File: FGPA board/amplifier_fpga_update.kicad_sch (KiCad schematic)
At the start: 10 parts, among them U1 LFXP2-5E-5TN144, U3 MCP4921

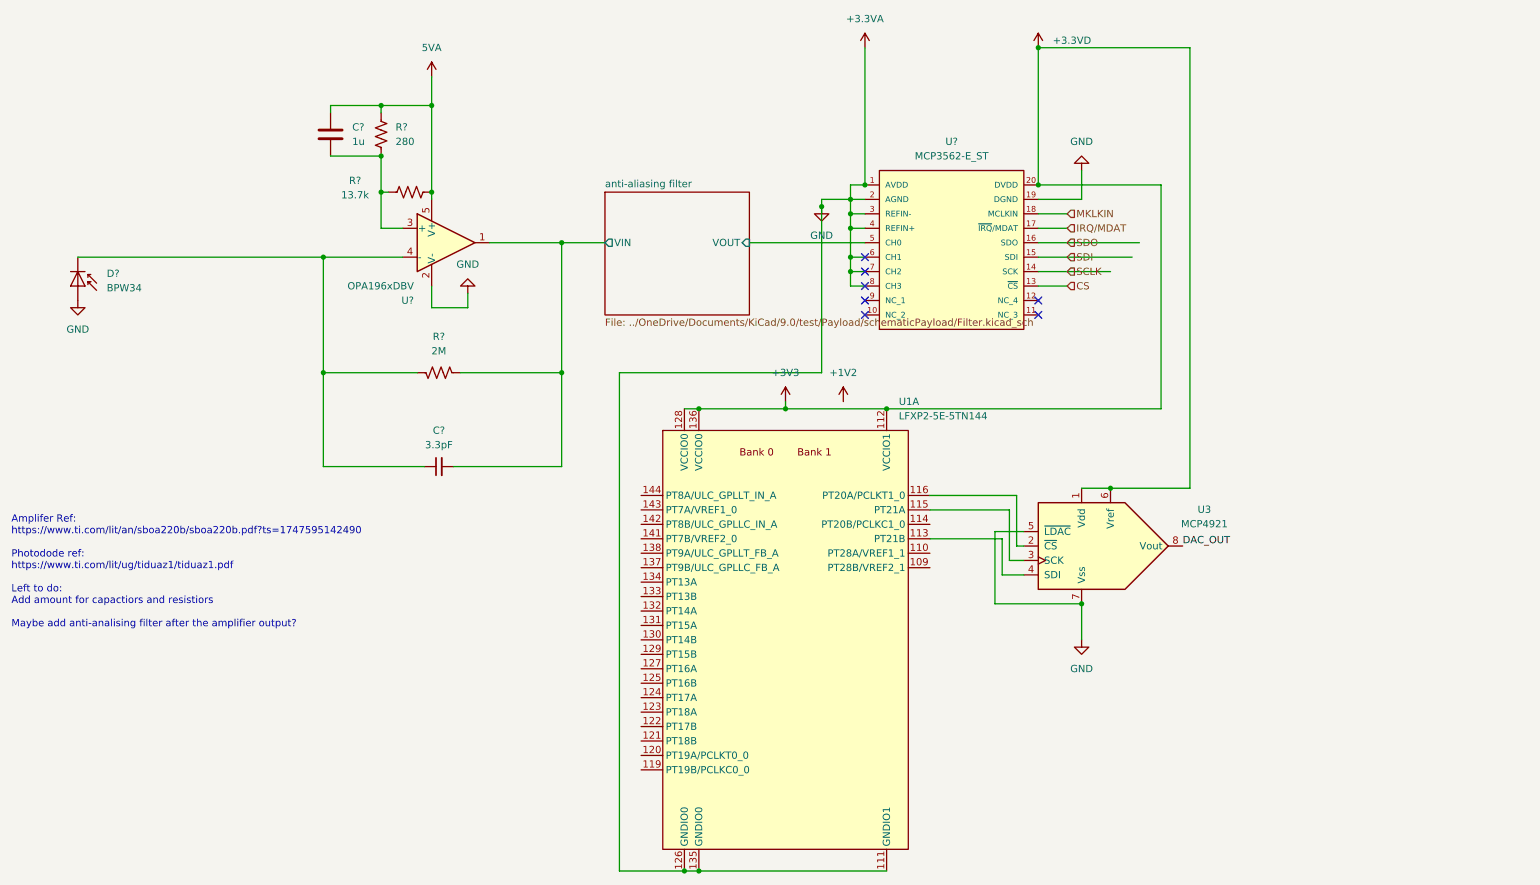
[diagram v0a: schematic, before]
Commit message: Add files via upload
Added SPI Flash, decoupling capacitors to ADC, decoupling to FPGA power pins and VCCPLL,
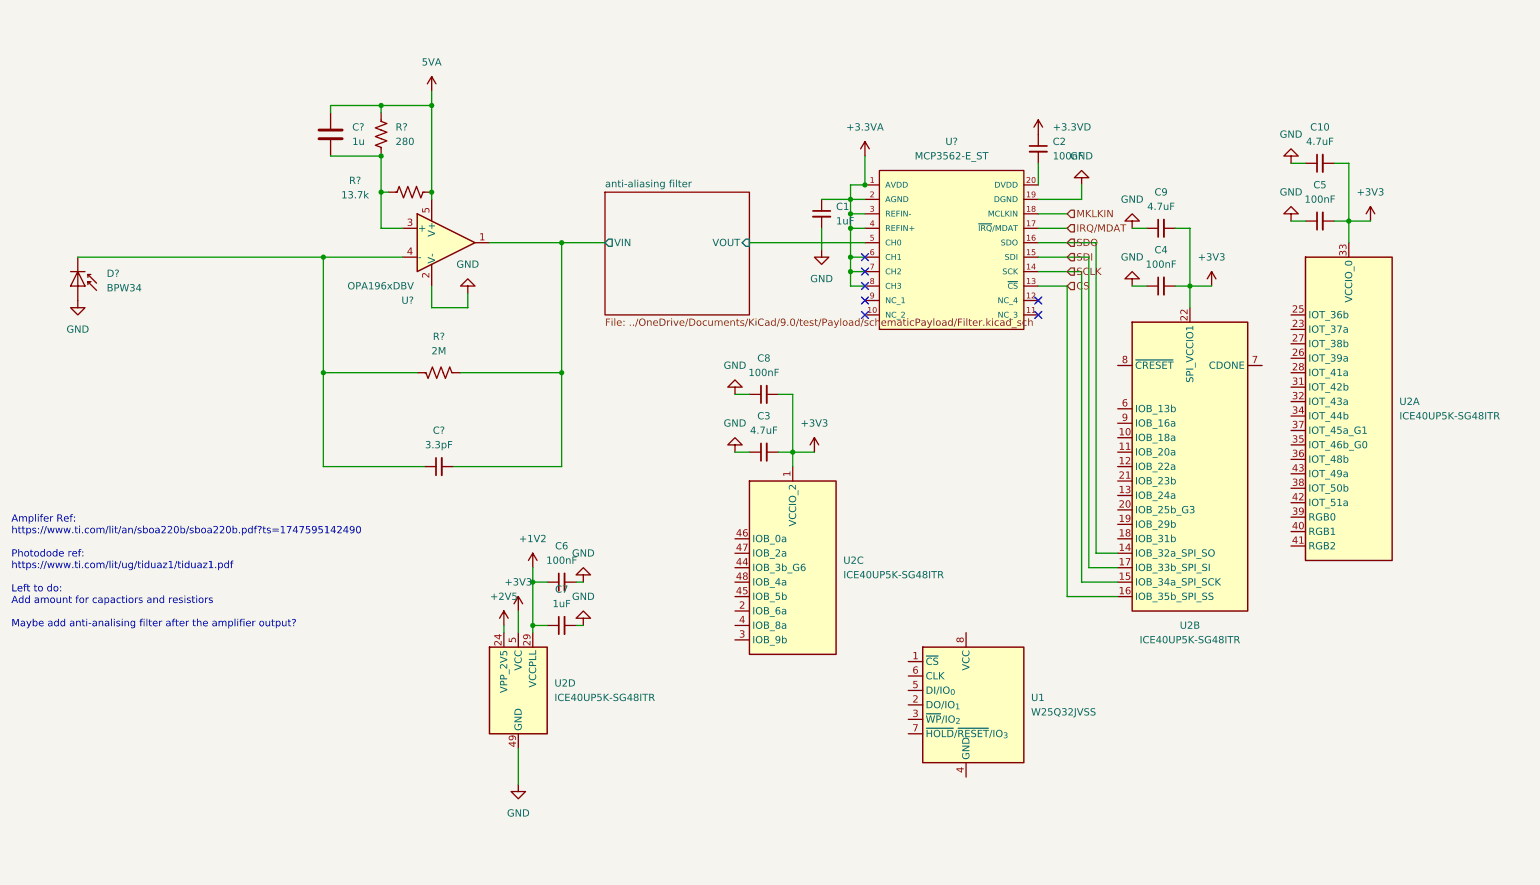
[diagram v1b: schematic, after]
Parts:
- removed U1: LFXP2-5E-5TN144, Package_QFP:TQFP-144_20x20mm_P0.5mm, symbol FPGA_Lattice:LFXP2-5E-5TN144
- removed U3: MCP4921, symbol Analog_DAC:MCP4921
- added C1, C7: 1uF, symbol Device:C_Small
- added C10, C3, C9: 4.7uF, symbol Device:C_Small
- added C2, C4, C5, C6, C8: 100nF, symbol Device:C_Small
- added U1: W25Q32JVSS, Package_SO:SOIC-8_5.3x5.3mm_P1.27mm, symbol Memory_Flash:W25Q32JVSS
- added U2: ICE40UP5K-SG48ITR, Package_DFN_QFN:QFN-48-1EP_7x7mm_P0.5mm_EP5.6x5.6mm, symbol FPGA_Lattice:ICE40UP5K-SG48ITR
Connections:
- net +1V2: now also C6.1, C7.1, U2.29 (VCCPLL)
- net +3.3VA: now also C1.1; no longer D?.2 (A), U?.19 (DGND), U?.2 (V-)
- net +3.3VD: now also C2.1; no longer U?.20 (DVDD)
- net CS: now also U2.16 (IOB_35b_SPI_SS)
- net SCLK: now also U2.15 (IOB_34a_SPI_SCK)
- net SDI: now also U2.17 (IOB_33b_SPI_SI)
- net SDO: now also U2.14 (IOB_32a_SPI_SO)
- new net: C2.2, U?.20 (DVDD)
- new net +2V5: U2.24 (VPP_2V5)
- new net +3V3: C10.2, C3.2, C4.2, C5.2, C8.2, C9.2, U2.1 (VCCIO_2), U2.22 (SPI_VCCIO1), U2.30 (VCC), U2.33 (VCCIO_0), U2.5 (VCC)
- new net GND: C1.2, C10.1, C3.1, C4.1, C5.1, C6.2, C7.2, C8.1, C9.1, D?.2 (A), U2.49 (GND), U?.19 (DGND), U?.2 (V-)
